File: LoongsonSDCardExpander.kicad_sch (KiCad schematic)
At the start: 30 parts, among them J1 USB_C_Receptacle_USB2.0, J2 Micro_SD_Card_Det, J3 Conn_02x10_Odd_Even, U1 CH340E

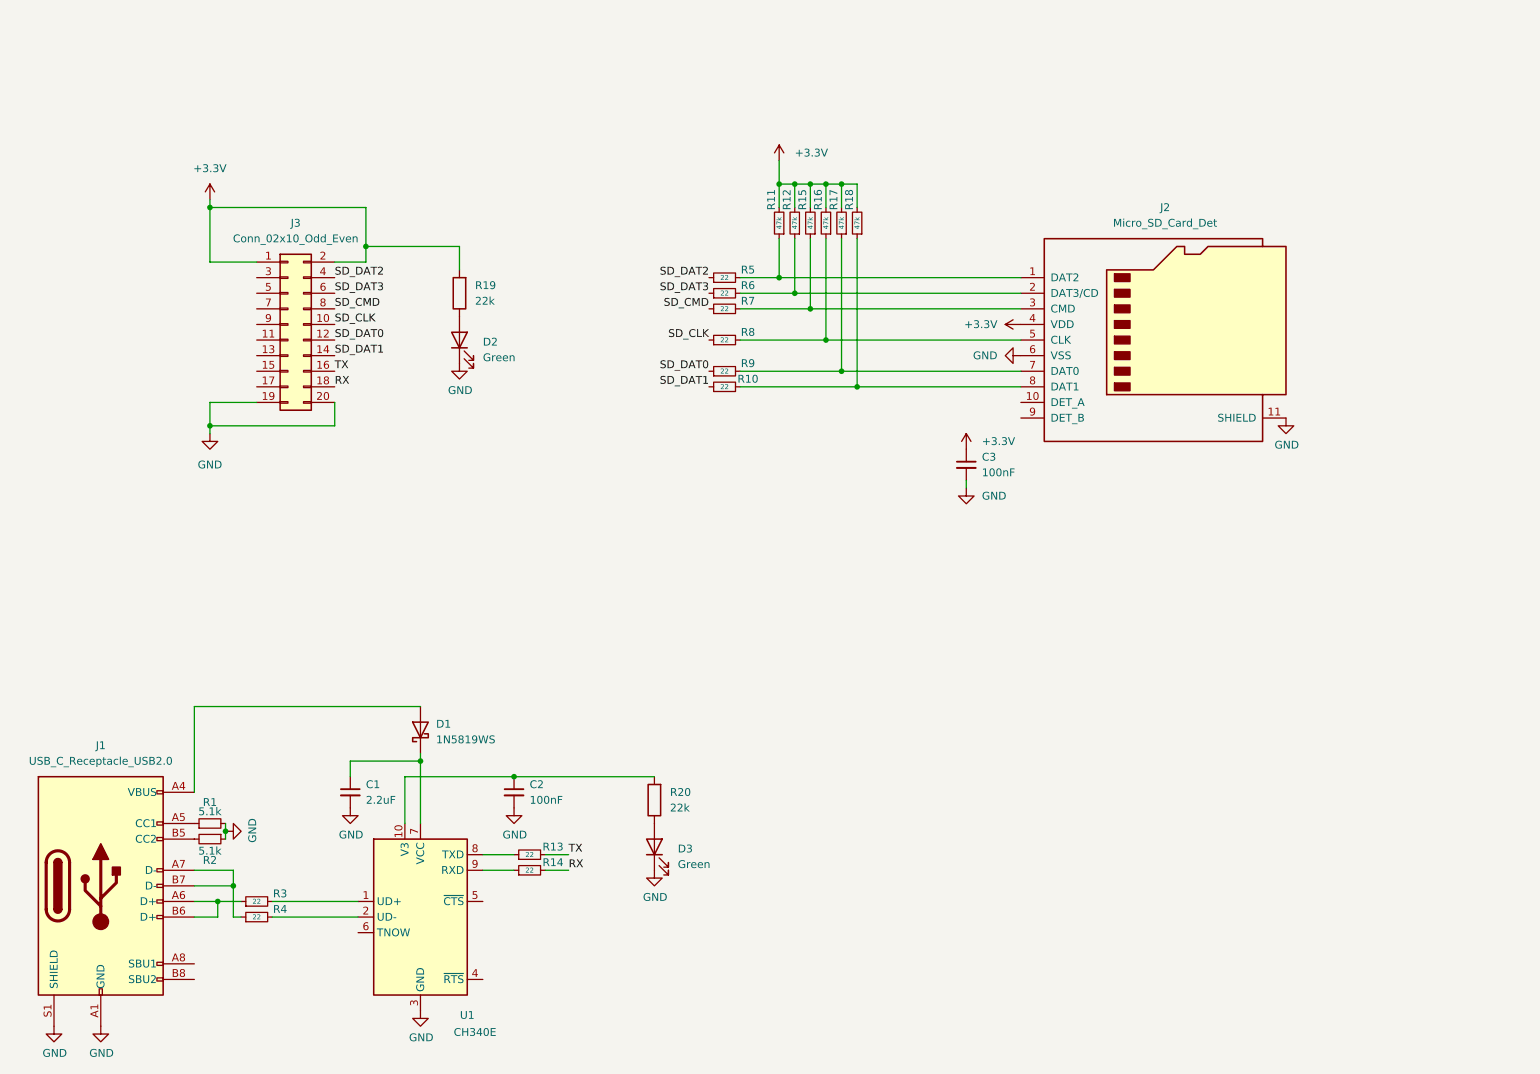
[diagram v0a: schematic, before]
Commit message: 添加Conn_01x11_Socket
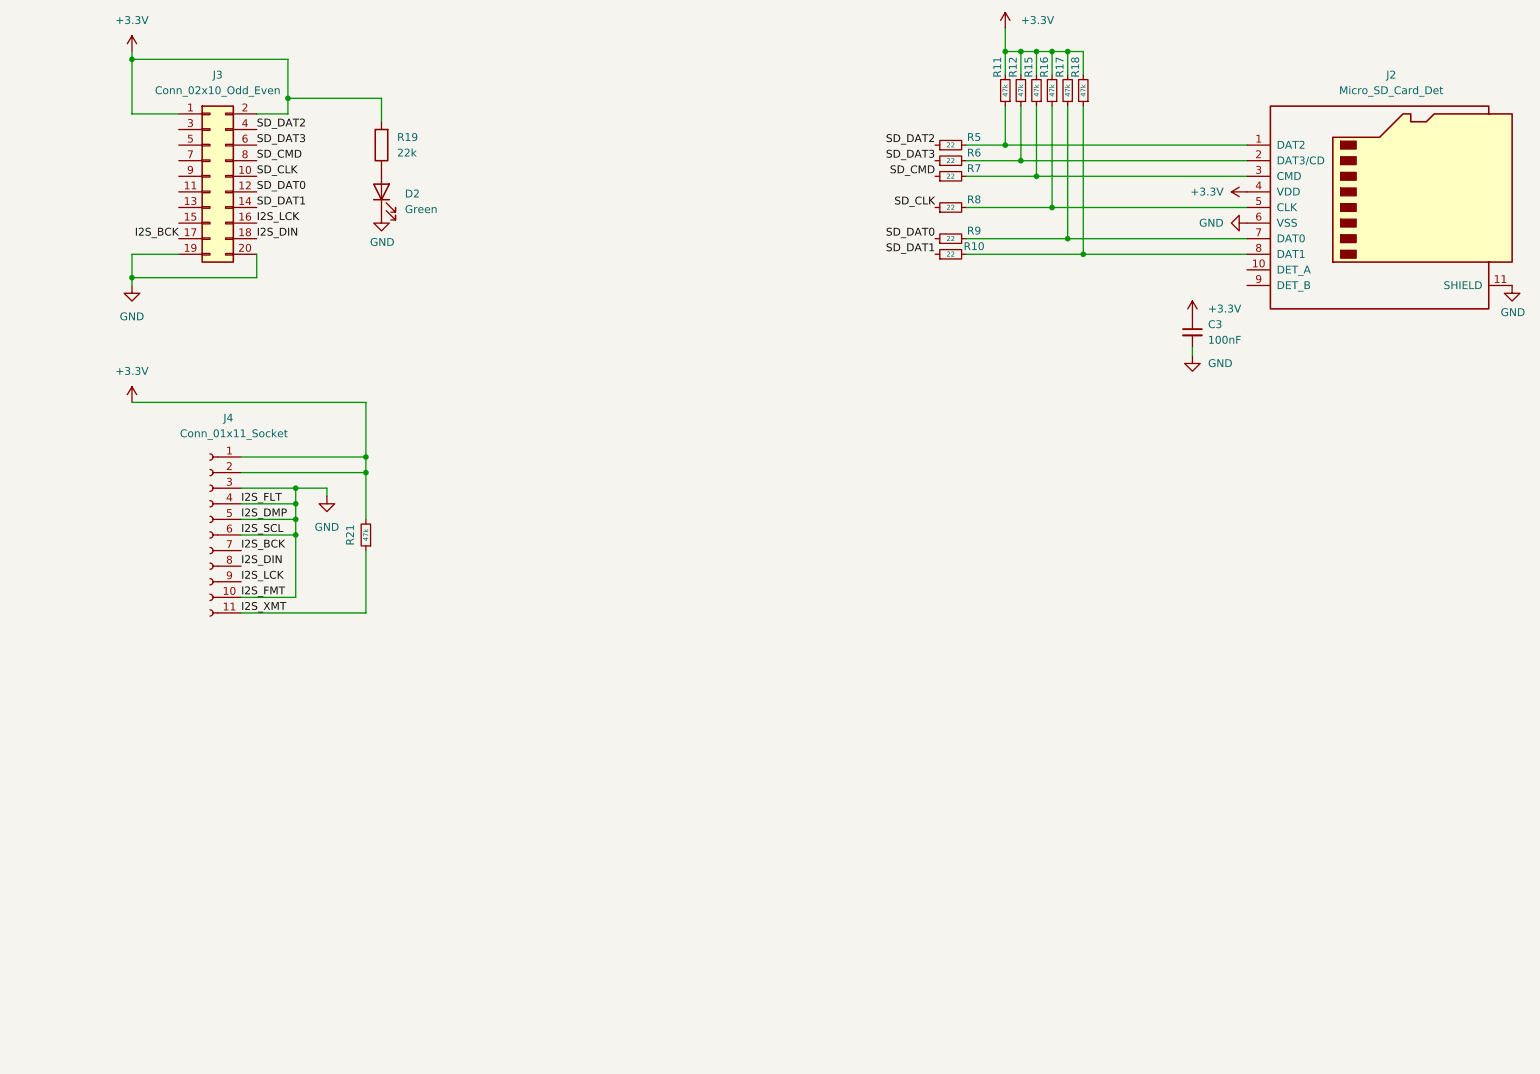
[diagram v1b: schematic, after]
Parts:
- removed C1: 2.2uF, lc:0402_C, symbol Device:C_Small
- removed C2: 100nF, lc:0402_C, symbol Device:C_Small
- removed D1: 1N5819WS, lc:SOD-323, symbol Diode:1N5819
- removed D3: Green, lc:0805_LED_S1_NUM, symbol Device:LED
- removed J1: USB_C_Receptacle_USB2.0, t123yh:USB_C_Receptacle_HRO_TYPE-C-31-M-12, symbol Connector:USB_C_Receptacle_USB2.0
- removed R1, R2: 5.1k, lc:0402_R, symbol Device:R_Small
- removed R13, R14, R3, R4: 22, lc:0402_R, symbol Device:R_Small
- removed R20: 22k, lc:0402_R, symbol Device:R
- removed U1: CH340E, Package_SO:MSOP-10_3x3mm_P0.5mm, symbol Interface_USB:CH340E
- added J4: Conn_01x11_Socket, Connector_PinSocket_2.54mm:PinSocket_1x11_P2.54mm_Vertical, symbol Connector:Conn_01x11_Socket
- added R21: 47k, lc:0402_R, symbol Device:R_Small
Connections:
- net +3.3V: now also J4.1 (Pin_1), J4.2 (Pin_2), R21.2
- net GND: now also J4.10 (Pin_10), J4.3 (Pin_3), J4.4 (Pin_4), J4.5 (Pin_5), J4.6 (Pin_6)
- net I2S_BCK: now reaches J3.17 (Pin_17)
- net I2S_BCK: now also J4.7 (Pin_7)
- net RX renamed I2S_DIN
- net I2S_DIN: now also J4.8 (Pin_8)
- net TX renamed I2S_LCK
- net I2S_LCK: now also J4.9 (Pin_9)
- new net I2S_XMT: J4.11 (Pin_11), R21.1
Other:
- moved on the sheet: C3, D2, J2, J3, R10, R11, R12, R15, R16, R17, R18, R19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
